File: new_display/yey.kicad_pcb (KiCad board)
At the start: 2 copper layers, 100 x 60 mm, 31 parts, among them J1 Screw_Terminal_2x2.54, J3 FH34SRJ-24S-0.5SH_99_, Q1 ZXM61N03F, Q3 ZXM61N03F, SW2 Button-THT - 2-1825910-7

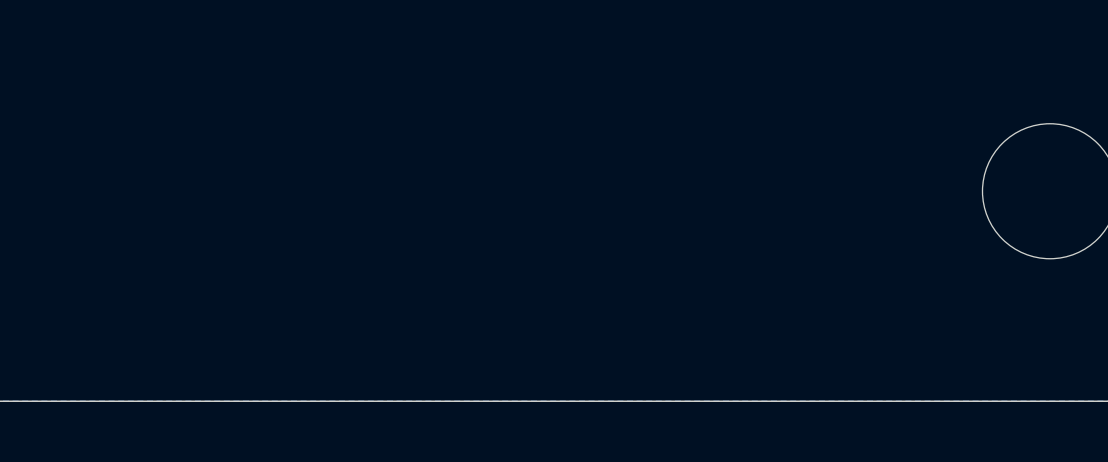
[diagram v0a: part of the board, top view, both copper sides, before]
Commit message: Silk screen names
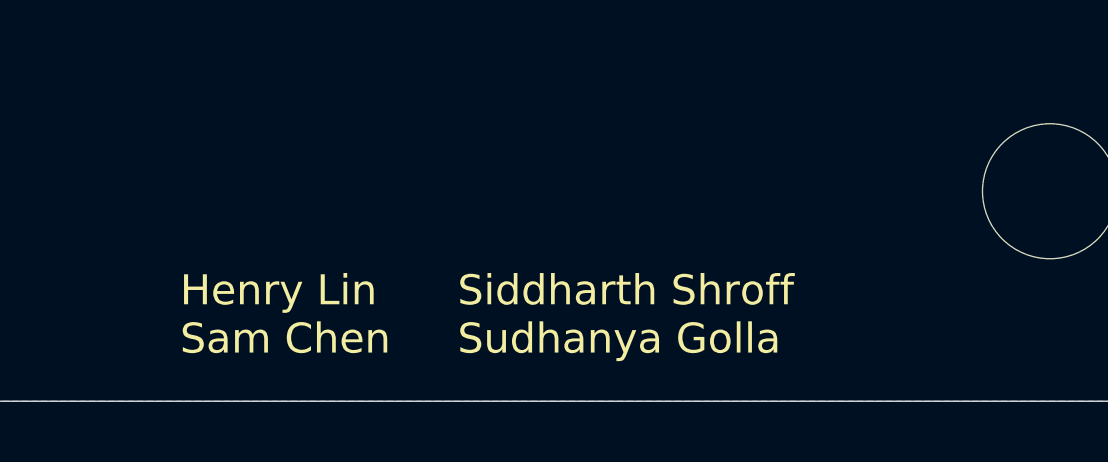
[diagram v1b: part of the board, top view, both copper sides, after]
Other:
- board text added: "Henry Lin Sam Chen"
- board text added: "Siddharth Shroff Sudhanya Golla"
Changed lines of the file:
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@@
 		(layer "Edge.Cuts")
+	)
+	(gr_text "Henry Lin\nSam Chen  "
+		(at 212 131 0)
+		(layer "F.SilkS")
+		(effects
+			(font
+				(size 1 1)
+				(thickness 0.1)
+			)
+			(justify left bottom)
+		)
+	)
+	(gr_text "Siddharth Shroff\nSudhanya Golla  "
+		(at 221.25 131 0)
+		(layer "F.SilkS")
+		(effects
+			(font
+				(size 1 1)
+				(thickness 0.1)
+			)
+			(justify left bottom)
+		)
 	)
 	(segment
